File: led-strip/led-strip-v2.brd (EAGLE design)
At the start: 117.5 x 8.7 mm, 21 parts

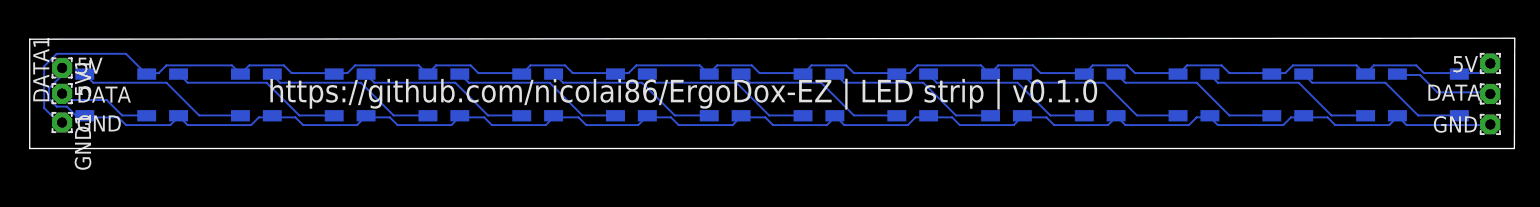
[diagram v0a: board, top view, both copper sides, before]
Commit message: add v0.2.0 with decoupling capacitors between leds
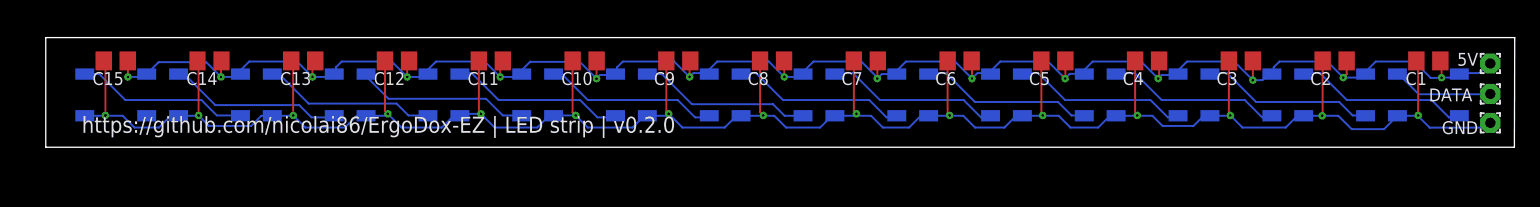
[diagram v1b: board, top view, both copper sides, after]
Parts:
- removed 5V1, DATA1, GND1: (no value), wirepad:1,6/0,8
- added C1, C10, C11, C12, C13, C14, C15, C2, C3, C4, C5, C6, C7, C8, C9: (no value), rcl:C0805
- LED1: device 1655:WS2812B_1 -> sk6812:WS2812B_1
- moved GND 0.13 mm to (117.0, 2.46)
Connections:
- removed net S$1: DATA1.1, LED15.2
- net +5V: now also C1.1, C10.1, C11.1, C12.1, C13.1, C14.1, C15.1, C2.1, C3.1, C4.1, C5.1, C6.1, C7.1, C8.1, C9.1; no longer GND1.1
- net GND: now also C1.2, C10.2, C11.2, C12.2, C13.2, C14.2, C15.2, C2.2, C3.2, C4.2, C5.2, C6.2, C7.2, C8.2, C9.2; no longer 5V1.1
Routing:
- net GND: track 127.2 -> 188.7 mm, vias 0 -> 15
- net +5V: track 129.2 -> 150.4 mm, vias 0 -> 15
- net S$1: track 7.42 -> 0.00 mm
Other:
- board size 117.5 x 8.7 mm -> 116.3 x 8.7 mm
- board text added: "https://github.com/nicolai86/ErgoDox-EZ | LED strip | v0.2.0"
- board text removed: "5V"
- board text removed: "DATA"
- board text removed: "GND"
- board text removed: "https://github.com/nicolai86/ErgoDox-EZ | LED strip | v0.1.0"
